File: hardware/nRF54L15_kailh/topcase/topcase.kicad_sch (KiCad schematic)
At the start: 88 parts

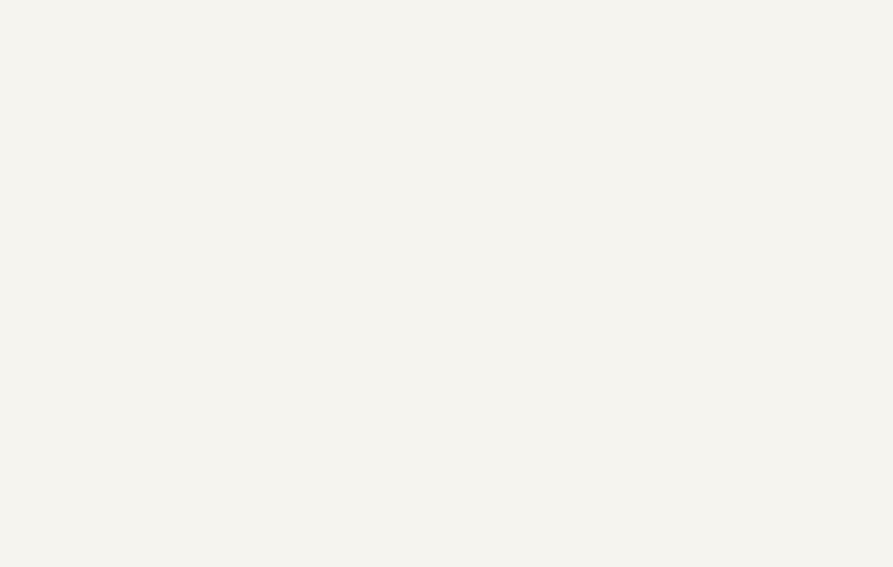
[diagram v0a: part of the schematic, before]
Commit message: A  hardware/nRF54L15_kailh/.gitignore M  hardware/nRF54L15_kailh/border.py A  hardware/nRF54L15_kailh/botcase/botcase-Edge_Cuts.dxf A  hardware/nRF54L15_kailh/botcase/botcase-Edge_Cuts.gm1 A  hardware/nRF54L15_kailh/botcase/botcase-Edge_Cuts.svg A  hardware/nRF54L15_kailh/botcase/botcase.kicad_pcb A  hardware/nRF54L15_kailh/botcase/botcase.kicad_prl A  hardware/nRF54L15_kailh/botcase/botcase.kicad_pro A  hardware/nRF54L15_kailh/botcase/botcase.kicad_sch A  hardware/nRF54L15_kailh/botcase/fp-lib-table A  hardware/nRF54L15_kailh/botcase/sym-lib-table A  hardware/nRF54L15_kailh/kerf.py D  hardware/nRF54L15_kailh/pat1.kicad_mod D  hardware/nRF54L15_kailh/pat1.kicad_sym D  hardware/nRF54L15_kailh/pat2.kicad_mod D  hardware/nRF54L15_kailh/pat3.kicad_mod D  hardware/nRF54L15_kailh/pat4.kicad_mod D  hardware/nRF54L15_kailh/pat5.kicad_mod D  hardware/nRF54L15_kailh/pcb/pcb-Edge_Cuts.dxf D  hardware/nRF54L15_kailh/pcb/pcb-F_Fab.dxf D  hardware/nRF54L15_kailh/pcb/pcb-User_3.dxf D  hardware/nRF54L15_kailh/pcb/pcb-User_5.dxf D  hardware/nRF54L15_kailh/pcb/pcb-User_6.dxf M  hardware/nRF54L15_kailh/placefp.py M  hardware/nRF54L15_kailh/swplate/swplate.kicad_pcb M  hardware/nRF54L15_kailh/swplate/swplate.kicad_prl M  hardware/nRF54L15_kailh/swplate/swplate.kicad_sch A  hardware/nRF54L15_kailh/test.py R  hardware/nRF54L15_kailh/tmr-footprints/DowelHole_2.9mm_M3_powdercoat.kicad_mod -> hardware/nRF54L15_kailh/tmr-footprints/DowelHole_2.8mm_M3_powdercoat.kicad_mod R  hardware/nRF54L15_kailh/tmr-footprints/DowelHole_3.0mm_M3_powdercoat.kicad_mod -> hardware/nRF54L15_kailh/tmr-footprints/PilotHole_2.05mm_M2.5_tap.kicad_mod A  hardware/nRF54L15_kailh/tmr-footprints/RivetClearanceHole_1.5mm.kicad_mod A  hardware/nRF54L15_kailh/tmr-footprints/RivetInterferenceHole_1.3mm_drill_to_1.35mm.kicad_mod M  hardware/nRF54L15_kailh/tmr-footprints/Switch_Cutout_dummy.kicad_mod D  hardware/nRF54L15_kailh/tmr-footprints/pat1.kicad_mod M  hardware/nRF54L15_kailh/topcase/topcase.kicad_pcb M  hardware/nRF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
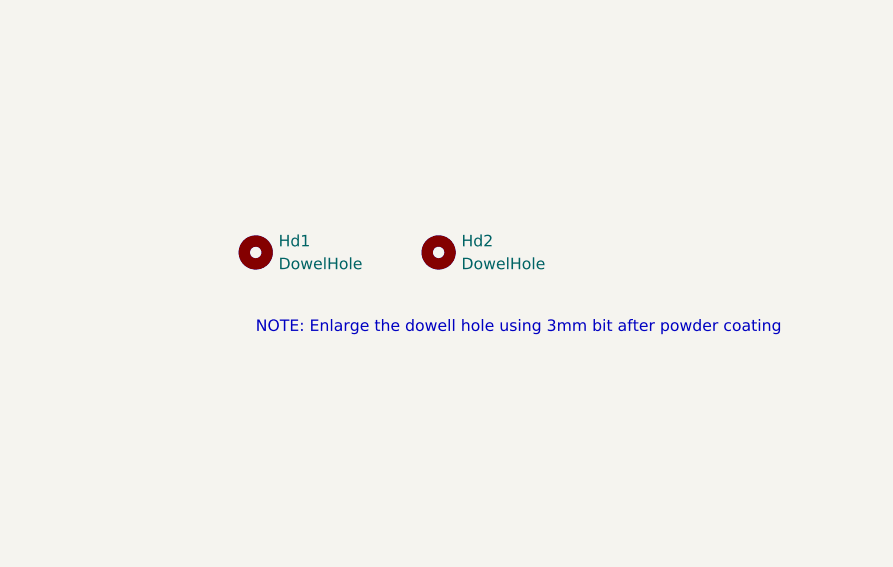
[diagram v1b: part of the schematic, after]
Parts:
- added Hd1, Hd2: DowelHole, tmr-lib:DowelHole_2.8mm_M3_powdercoat, symbol Mechanical:MountingHole
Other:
- note added: "NOTE: Enlarge the dowell hole using 3mm bit after powder coating"
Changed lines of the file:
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@@
 	(generator_version "9.0")
 	(paper "A4")
+	(text "NOTE: Enlarge the dowell hole using 3mm bit after powder coating"
+		(exclude_from_sim no)
+		(at 208.28 151.892 0)
+		(effects
+			(font
+				(size 1.27 1.27)
+			)
+		)
+	)
 	(symbol
 		(lib_id "tmr-lib:SWHole")
@@
 	)
 	(symbol
+		(lib_id "Mechanical:MountingHole")
+		(at 199.39 143.51 0)
+		(unit 1)
+		(exclude_from_sim no)
+		(in_bom no)
+		(on_board yes)
+		(dnp no)
+		(fields_autoplaced yes)
+		(property "Reference" "Hd2"
+			(at 201.93 142.2399 0)
+			(effects
+				(font
+					(size 1.27 1.27)
+				)
+				(justify left)
+			)
+		)
+		(property "Value" "DowelHole"
+			(at 201.93 144.7799 0)
+			(effects
+				(font
+					(size 1.27 1.27)
+				)
+				(justify left)
+			)
+		)
+		(property "Footprint" "tmr-lib:DowelHole_2.8mm_M3_powdercoat"
+			(at 199.39 143.51 0)
+			(effects
+				(font
+					(size 1.27 1.27)
+				)
+				(hide yes)
+			)
+		)
+		(property "Datasheet" "~"
+			(at 199.39 143.51 0)
+			(effects
+				(font
+					(size 1.27 1.27)
+				)
+				(hide yes)
+			)
+		)
+		(property "Description" "Mounting Hole without connection"
+			(at 199.39 143.51 0)
+			(effects
+				(font
+					(size 1.27 1.27)
+				)
+				(hide yes)
+			)
+		)
+		(instances
+			(project "topcase"
+				(path "/4c67809e-1748-4898-89f6-ff92314048f2"
+					(reference "Hd2")
+					(unit 1)
+				)
+			)
+		)
+	)
+	(symbol
 		(lib_id "tmr-lib:SWHole")
 		(at 91.44 53.34 0)
@@
 					(unit 1)
 				)
+			)
+		)
+	)
+	(symbol
+		(lib_id "Mechanical:MountingHole")
+		(at 179.07 143.51 0)
+		(unit 1)
+		(exclude_from_sim no)
+		(in_bom no)
+		(on_board yes)
+		(dnp no)
+		(fields_autoplaced yes)
+		(property "Reference" "Hd1"
+			(at 181.61 142.2399 0)
+			(effects
+				(font
+					(size 1.27 1.27)
+				)
+				(justify left)
+			)
+		)
+		(property "Value" "DowelHole"
+			(at 181.61 144.7799 0)
+			(effects
+				(font
+					(size 1.27 1.27)
+				)
+				(justify left)
+			)
+		)
+		(property "Footprint" "tmr-lib:DowelHole_2.8mm_M3_powdercoat"
+			(at 179.07 143.51 0)
+			(effects
+				(font
+					(size 1.27 1.27)
+				)
+				(hide yes)
+			)
+		)
+		(property "Datasheet" "~"
+			(at 179.07 143.51 0)
+			(effects
+				(font
+					(size 1.27 1.27)
+				)
+				(hide yes)
+			)
+		)
+		(property "Description" "Mounting Hole without connection"
+			(at 179.07 143.51 0)
+			(effects
+				(font
+					(size 1.27 1.27)
+				)
+				(hide yes)
+			)
+		)
+		(instances
+			(project "topcase"
+				(path "/4c67809e-1748-4898-89f6-ff92314048f2"
+					(reference "Hd1")
+					(unit 1)
+				)
